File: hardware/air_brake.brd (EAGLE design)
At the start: 100 x 80 mm, 18 parts

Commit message: updated cap values
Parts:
- C1, C2, C3, C4: value 33uF -> .22uF
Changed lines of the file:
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@@
 <attribute name="VALUE" x="-1.524" y="-59.309" size="1.778" layer="27" ratio="10" rot="R90"/>
 </element>
-<element name="C1" library="adafruit" library_urn="urn:adsk.eagle:library:420" package="C025-040X050" package3d_urn="urn:adsk.eagle:package:6240321/1" value="33uF" x="-22.86" y="-55.88" smashed="yes">
+<element name="C1" library="adafruit" library_urn="urn:adsk.eagle:library:420" package="C025-040X050" package3d_urn="urn:adsk.eagle:package:6240321/1" value=".22uF" x="-22.86" y="-55.88" smashed="yes">
 <attribute name="NAME" x="-25.146" y="-53.721" size="1.27" layer="25" ratio="10"/>
 <attribute name="VALUE" x="-25.146" y="-59.309" size="1.27" layer="27" ratio="10"/>
 </element>
-<element name="C2" library="adafruit" library_urn="urn:adsk.eagle:library:420" package="C025-040X050" package3d_urn="urn:adsk.eagle:package:6240321/1" value="33uF" x="-31.75" y="-55.88" smashed="yes">
+<element name="C2" library="adafruit" library_urn="urn:adsk.eagle:library:420" package="C025-040X050" package3d_urn="urn:adsk.eagle:package:6240321/1" value=".22uF" x="-31.75" y="-55.88" smashed="yes">
 <attribute name="NAME" x="-34.036" y="-53.721" size="1.27" layer="25" ratio="10"/>
 <attribute name="VALUE" x="-34.036" y="-59.309" size="1.27" layer="27" ratio="10"/>
 </element>
-<element name="C3" library="adafruit" library_urn="urn:adsk.eagle:library:420" package="C025-040X050" package3d_urn="urn:adsk.eagle:package:6240321/1" value="33uF" x="-40.64" y="-55.88" smashed="yes">
+<element name="C3" library="adafruit" library_urn="urn:adsk.eagle:library:420" package="C025-040X050" package3d_urn="urn:adsk.eagle:package:6240321/1" value=".22uF" x="-40.64" y="-55.88" smashed="yes">
 <attribute name="NAME" x="-42.926" y="-53.721" size="1.27" layer="25" ratio="10"/>
 <attribute name="VALUE" x="-42.926" y="-59.309" size="1.27" layer="27" ratio="10"/>
 </element>
-<element name="C4" library="adafruit" library_urn="urn:adsk.eagle:library:420" package="C025-040X050" package3d_urn="urn:adsk.eagle:package:6240321/1" value="33uF" x="-49.53" y="-55.88" smashed="yes">
+<element name="C4" library="adafruit" library_urn="urn:adsk.eagle:library:420" package="C025-040X050" package3d_urn="urn:adsk.eagle:package:6240321/1" value=".22uF" x="-49.53" y="-55.88" smashed="yes">
 <attribute name="NAME" x="-51.816" y="-53.721" size="1.27" layer="25" ratio="10"/>
 <attribute name="VALUE" x="-51.816" y="-59.309" size="1.27" layer="27" ratio="10"/>

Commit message: very rough prelim board layout
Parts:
- moved C3 167.0 mm to (88.9, 49.5), turned to 270 degrees
- moved C4 165.0 mm to (77.5, 49.5), turned to 180 degrees
- moved C1 148.5 mm to (88.9, 41.9), turned to 90 degrees
- moved 3V3_REG 146.2 mm to (83.8, 64.8)
- moved C2 144.8 mm to (76.2, 40.6), turned to 270 degrees
- moved R5 128.4 mm to (45.7, 25.4), turned to 180 degrees
- moved 5V_REG 106.3 mm to (83.8, 25.4), turned to 180 degrees
- moved LED1 74.7 mm to (26.7, 44.5)
- moved LED2 73.5 mm to (26.7, 38.1)
- moved LED3 72.3 mm to (26.7, 31.8), flipped to the bottom, turned to 180 degrees
- moved R2 63.1 mm to (58.4, 25.4), turned to 180 degrees
- moved R4 51.8 mm to (33.0, 21.6), turned to 180 degrees
- moved R3 49.7 mm to (33.0, 25.4), turned to 180 degrees
- moved R1 46.6 mm to (71.1, 25.4)
- moved JP4 24.4 mm to (57.8, 52.1)
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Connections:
- net N$1: now also TEENSY4.0.11; no longer TEENSY4.0.3
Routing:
- net GND: track 0.00 -> 150.9 mm, vias 0 -> 5
- net +3V3: track 0.00 -> 64.4 mm
- net +5V: track 0.00 -> 32.5 mm
- net N$3: track 0.00 -> 21.9 mm
- net V_BATT: track 0.00 -> 20.5 mm
- net N$5: track 0.00 -> 17.9 mm
- net N$4: track 0.00 -> 17.6 mm
- net N$7: track 0.00 -> 12.7 mm
- net N$6: track 0.00 -> 9.94 mm
- net N$1: track 0.00 -> 7.62 mm
- net N$2: track 0.00 -> 5.08 mm
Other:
- board size 100 x 80 mm -> 182.6 x 85.1 mm
- board text removed: "9-Axis Abs. Orientation"
- board text removed: "Altimeter"
- board text removed: "BNO055"
- board text removed: "GND"
- board text removed: "INT1"
- board text removed: "INT2"
- board text removed: "MPL3115A2"
- board text removed: "RST"
- board text removed: "SCL"
- board text removed: "Vin"

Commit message: began power routing
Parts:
- moved C1 1.27 mm to (88.9, 40.6)
- turned C2 to 90 degrees
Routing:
- net +3V3: track 64.4 -> 12.7 mm
- net N$3: track 21.9 -> 0.00 mm
- net GND: track 150.9 -> 130.6 mm, vias 5 -> 0
- net N$5: track 17.9 -> 0.00 mm
- net N$4: track 17.6 -> 0.00 mm
- net N$7: track 12.7 -> 0.00 mm
- net N$6: track 9.94 -> 0.00 mm
- net N$1: track 7.62 -> 0.00 mm
- net N$2: track 5.08 -> 0.00 mm
- net +5V: track 32.5 -> 36.2 mm
- removed copper zone on layer 1, net GND
- removed copper zone on layer 16, net GND
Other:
- outline, holes or cut-outs redrawn

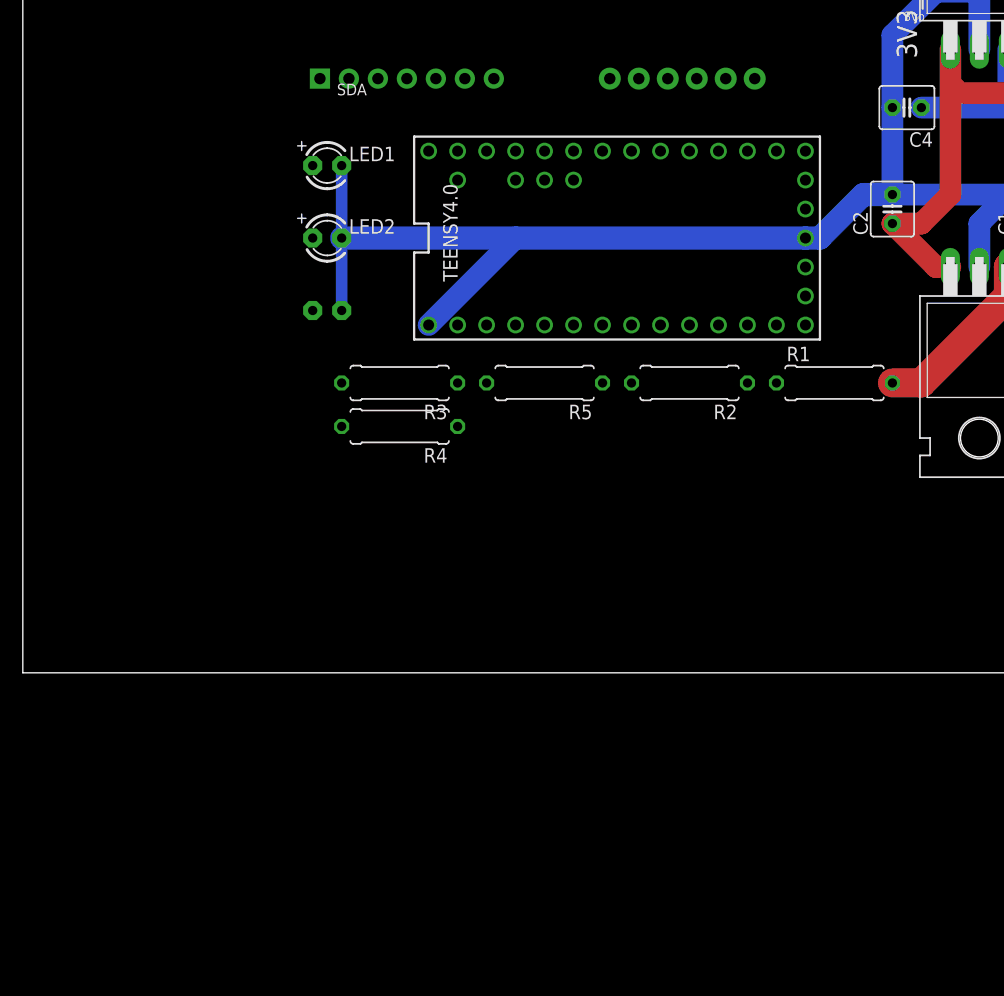
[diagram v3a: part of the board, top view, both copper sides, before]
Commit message: updated to reflect no logging
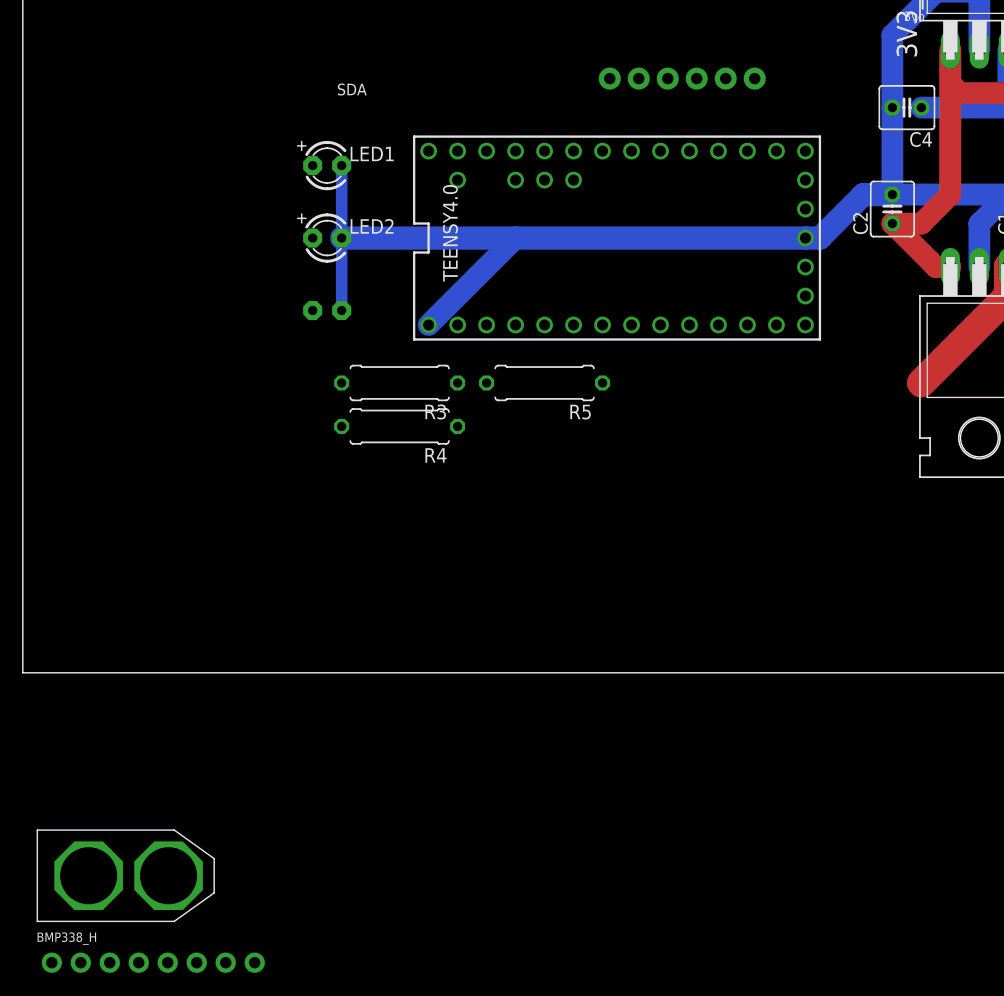
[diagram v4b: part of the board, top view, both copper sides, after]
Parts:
- removed JP1: (no value), microbuilder:1X07_ROUND_70
- removed R1, R2: 1M, resistor:0309/10
- added BMP338_H: (no value), microbuilder:1X08_ROUND_70
- added U$1: XT60, XT60:XT60
- C1, C2, C3, C4: value .22uF -> 22uF
- R3, R4, R5: value 560 -> 1k
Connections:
- net N$2 renamed LED_1
- net N$6 renamed LED_2
- net N$7 renamed LED_3
- removed net N$1: R1.1, R2.1, TEENSY4.0.11
- removed net SCL_5V: JP1.6, JP4.5, TEENSY4.0.19/A5
- removed net SDA_5V: JP1.7, JP4.4, TEENSY4.0.18/A4
- new net BATT_TEMP: TEENSY4.0.A11
- new net BATT_VSENSE: TEENSY4.0.14/A0
- new net CS: BMP338_H.7
- new net INT: BMP338_H.8
- new net MD_CS1: TEENSY4.0.6
- new net MD_CS2: TEENSY4.0.8
- new net MD_EN1: TEENSY4.0.5
- new net MD_EN2: TEENSY4.0.7
- new net MD_PWM1: TEENSY4.0.20/A6
- new net MD_PWM2: TEENSY4.0.4
- new net SCL: BMP338_H.4, JP4.5, TEENSY4.0.19/A5
- new net SDA: BMP338_H.6, JP4.4, TEENSY4.0.18/A4
- net +3V3: now also BMP338_H.1; no longer JP1.3
- net +5V: no longer JP1.1
- net GND: now also BMP338_H.3, U$1.-; no longer JP1.2, R2.2
- net V_BATT: now also U$1.+; no longer R1.2
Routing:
- net V_BATT: track 20.7 -> 18.2 mm
